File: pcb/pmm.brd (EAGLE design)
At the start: 12.6 x 18 mm, 20 parts, among them IC3 STM32F042F4, SW3 324_SW, SW4 324_SW, U2 USBC_16P, U4 XC6206_DEV

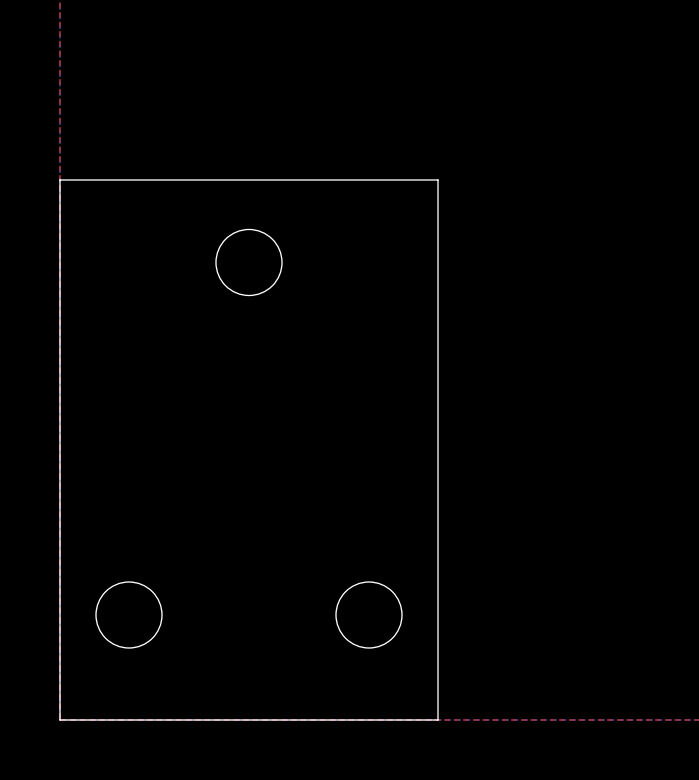
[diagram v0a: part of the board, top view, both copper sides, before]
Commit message: hotshoe done
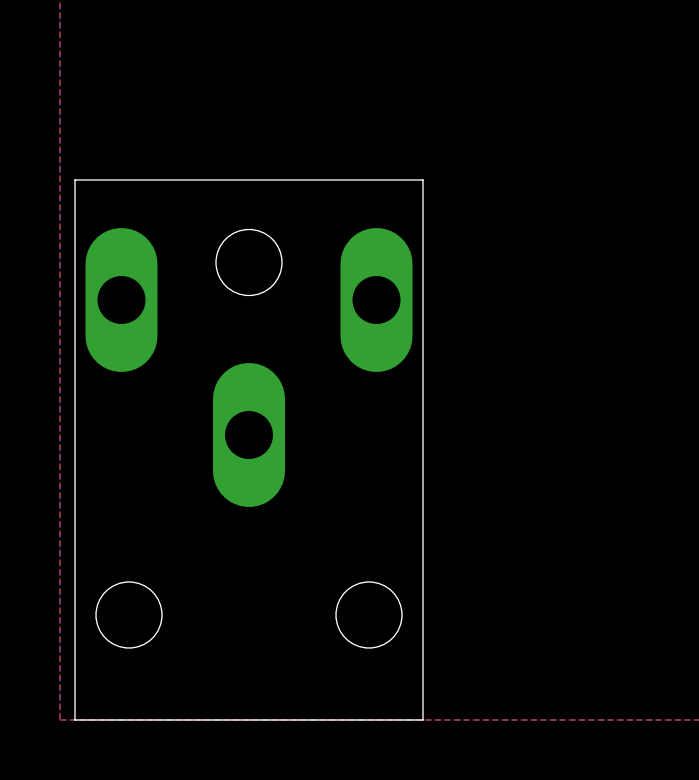
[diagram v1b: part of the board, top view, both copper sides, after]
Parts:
- added U$3, U$4, U$5: POGO_1.5MM_HOLE, apricot:POGO_1.5
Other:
- board size 12.6 x 18 mm -> 11.6 x 18 mm
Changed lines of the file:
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@@
 <setting verticaltext="up"/>
 </settings>
-<grid distance="1" unitdist="mm" unit="mm" style="lines" multiple="1" display="no" altdistance="1" altunitdist="mil" altunit="mil"/>
+<grid distance="0.5" unitdist="mm" unit="mm" style="lines" multiple="1" display="no" altdistance="1" altunitdist="mil" altunit="mil"/>
 <layers>
 <layer number="1" name="Top" color="4" fill="1" visible="no" active="yes"/>
@@
 <layer number="117" name="secv21" color="7" fill="1" visible="no" active="yes"/>
 <layer number="118" name="Rect_Pads" color="7" fill="1" visible="no" active="yes"/>
+<layer number="119" name="PF_Ref" color="7" fill="1" visible="yes" active="yes"/>
 <layer number="120" name="120" color="7" fill="1" visible="no" active="yes"/>
 <layer number="121" name="_tsilk" color="7" fill="1" visible="no" active="yes"/>
@@
 <layer number="131" name="tAdjust" color="7" fill="1" visible="no" active="yes"/>
 <layer number="132" name="bAdjust" color="7" fill="1" visible="no" active="yes"/>
+<layer number="133" name="bottom_silk" color="7" fill="1" visible="yes" active="yes"/>
+<layer number="134" name="silk_top" color="7" fill="1" visible="yes" active="yes"/>
+<layer number="135" name="silk_bottom" color="7" fill="1" visible="yes" active="yes"/>
+<layer number="136" name="silktop" color="7" fill="1" visible="yes" active="yes"/>
+<layer number="137" name="silkbottom" color="7" fill="1" visible="yes" active="yes"/>
+<layer number="138" name="EEE" color="7" fill="1" visible="yes" active="yes"/>
+<layer number="139" name="_tKeepout" color="7" fill="1" visible="yes" active="yes"/>
+<layer number="140" name="mbKeepout" color="7" fill="1" visible="yes" active="yes"/>
+<layer number="141" name="ASSEMBLY_TOP" color="7" fill="1" visible="yes" active="yes"/>
+<layer number="142" name="mbRestrict" color="7" fill="1" visible="yes" active="yes"/>
+<layer number="143" name="PLACE_BOUND_TOP" color="7" fill="1" visible="yes" active="yes"/>
 <layer number="144" name="Drill_legend" color="7" fill="1" visible="no" active="yes"/>
 <layer number="145" name="DrillLegend_01-02" color="7" fill="1" visible="no" active="yes"/>
@@
 <layer number="154" name="FabDoc2" color="7" fill="1" visible="no" active="yes"/>
 <layer number="155" name="FabDoc3" color="7" fill="1" visible="no" active="yes"/>
+<layer number="166" name="AntennaArea" color="7" fill="1" visible="yes" active="yes"/>
+<layer number="168" name="4mmHeightArea" color="7" fill="1" visible="yes" active="yes"/>
+<layer number="191" name="mNets" color="7" fill="1" visible="yes" active="yes"/>
+<layer number="192" name="mBusses" color="7" fill="1" visible="yes" active="yes"/>
+<layer number="193" name="mPins" color="7" fill="1" visible="yes" active="yes"/>
+<layer number="194" name="mSymbols" color="7" fill="1" visible="yes" active="yes"/>
+<layer number="195" name="mNames" color="7" fill="1" visible="yes" active="yes"/>
+<layer number="196" name="mValues" color="7" fill="1" visible="yes" active="yes"/>
 <layer number="199" name="Contour" color="7" fill="1" visible="no" active="yes"/>
 <layer number="200" name="200bmp" color="1" fill="10" visible="no" active="no"/>
@@
 <layer number="250" name="Descript" color="3" fill="1" visible="no" active="no"/>
 <layer number="251" name="SMDround" color="12" fill="11" visible="no" active="no"/>
+<layer number="253" name="Extra" color="7" fill="1" visible="yes" active="yes"/>
 <layer number="254" name="cooling" color="7" fill="1" visible="no" active="yes"/>
 <layer number="255" name="routoute" color="7" fill="1" visible="no" active="yes"/>
@@
 <board>
 <plain>
-<wire x1="0" y1="18" x2="0" y2="0" width="0" layer="20"/>
-<wire x1="0" y1="0" x2="12.6" y2="0" width="0" layer="20"/>
-<wire x1="12.6" y1="0" x2="12.6" y2="18" width="0" layer="20"/>
-<wire x1="12.6" y1="18" x2="0" y2="18" width="0" layer="20"/>
+<wire x1="0.5" y1="18" x2="0.5" y2="0" width="0" layer="20"/>
+<wire x1="0.5" y1="0" x2="12.1" y2="0" width="0" layer="20"/>
+<wire x1="12.1" y1="0" x2="12.1" y2="18" width="0" layer="20"/>
+<wire x1="12.1" y1="18" x2="0.5" y2="18" width="0" layer="20"/>
 <text x="60.325" y="54.61" size="0.889" layer="25">SCL</text>
 <text x="57.658" y="54.61" size="0.889" layer="25">SDA</text>
@@
 <attribute name="NAME" x="51.6852" y="49.5605" size="0.8128" layer="25"/>
 </element>
-<element name="U$12" library="3pos_slide_switch_centered" package="M2_SCREW_FOOT" value="M2_SCREW_DEV" x="6.3" y="15.25" smashed="yes"/>
-<element name="U$1" library="3pos_slide_switch_centered" package="M2_SCREW_FOOT" value="M2_SCREW_DEV" x="10.3" y="3.5" smashed="yes"/>
-<element name="U$2" library="3pos_slide_switch_centered" package="M2_SCREW_FOOT" value="M2_SCREW_DEV" x="2.3" y="3.5" smashed="yes"/>
+<element name="U$12" library="3pos_slide_switch_centered" package="M2_SCREW_FOOT" value="M2_SCREW_DEV" x="6.3" y="15.25" locked="yes" smashed="yes"/>
+<element name="U$1" library="3pos_slide_switch_centered" package="M2_SCREW_FOOT" value="M2_SCREW_DEV" x="10.3" y="3.5" locked="yes" smashed="yes"/>
+<element name="U$2" library="3pos_slide_switch_centered" package="M2_SCREW_FOOT" value="M2_SCREW_DEV" x="2.3" y="3.5" locked="yes" smashed="yes"/>
+<element name="U$3" library="apricot" package="POGO_1.5" value="POGO_1.5MM_HOLE" x="6.3" y="9.5" locked="yes" smashed="yes"/>
+<element name="U$4" library="apricot" package="POGO_1.5" value="POGO_1.5MM_HOLE" x="2.05" y="14" locked="yes" smashed="yes"/>
+<element name="U$5" library="apricot" package="POGO_1.5" value="POGO_1.5MM_HOLE" x="10.55" y="14" locked="yes" smashed="yes"/>
 </elements>
 <signals>

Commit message: working on PCB
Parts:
- added BT1: BU2032SM-G, BU2032SM-G:BAT_BU2032SM-G
- added C20, C21: 1uF, clock:0805
- added C22, C23: 2.2uF, clock:0805
- added J1: AUDIO_JACK_3.5MM_PTH, SparkFun-Connectors:AUDIO-JACK
- added J2: FFC3B07-05-T, FFC3B07-05-T:GCT_FFC3B07-05-T
- added R7: 390K, SparkFun-Passives:0805
- added R8: 5.1K, joyAnalog:0805
- added SW1: (no value), tx:SWITCH-SPST-SMD-A
- added U1: (no value), lul:LUL_UG-2864HSWEG01_1.3_WRAPAROUND
- C1, C2, C4: device clock:0805@1 -> clock:0805
- moved U2 73.6 mm to (52.7, -7.11), turned to 90 degrees
- moved LED2 2.92 mm to (48.2, 68.3)
- moved C2 2.92 mm to (63.4, 50.1)
- moved C4 2.92 mm to (66.5, 64.6)
- moved R6 2.92 mm to (48.1, 66.2)
- moved C1 2.92 mm to (66.5, 70.6)
- moved IC3 2.92 mm to (58.2, 48.3)
- moved LED1 2.92 mm to (48.2, 61.3)
- moved LED3 2.92 mm to (48.2, 54.3)
- moved R1 2.92 mm to (54.3, 62.5)
- moved R2 2.92 mm to (62.5, 62.5)
- moved R3 2.92 mm to (48.2, 52.3)
- moved R4 2.92 mm to (48.2, 59.3)
- moved R5 2.92 mm to (52.7, 47.3)
- moved SW3 2.92 mm to (68.2, 47.3)
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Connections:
- new net N$12: U1.12
- new net N$14: U1.11
- new net N$16: U1.10
- new net N$35: C20.2, U1.1
- new net N$36: C20.1, U1.2
- new net N$37: C21.2, U1.3
- new net N$38: C21.1, U1.4
- new net N$39: R7.2, U1.13
- new net N$40: C22.2, U1.14
- new net N$41: C23.2, U1.15
- new net N$43: R8.1, U1.9
- net +3V3: now also U1.5, U1.7
- net GND: now also C22.1, C23.1, R7.1, R8.2, U1.16, U1.17, U1.6
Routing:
- net N$6: track 35.6 -> 0.00 mm
- net +3V3: track 22.3 -> 0.00 mm, vias 5 -> 0
- net USB_DP: track 21.9 -> 0.00 mm
- net BUTTON1: track 19.9 -> 0.00 mm
- net USB_DN: track 19.9 -> 0.00 mm
- net +5V: track 19.0 -> 0.00 mm
- net N$4: track 15.9 -> 0.00 mm, vias 1 -> 0
- net BUTTON2: track 11.6 -> 0.00 mm
- net N$3: track 10.9 -> 0.00 mm, vias 1 -> 0
- net GND: track 5.07 -> 0.00 mm
- net N$33: track 3.52 -> 0.00 mm
- net N$31: track 2.87 -> 0.00 mm
- net N$29: track 2.14 -> 0.00 mm
- net N$5: track 2.06 -> 0.00 mm
- net N$1: track 2.06 -> 0.00 mm
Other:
- board size 11.6 x 18 mm -> 95.5 x 43 mm

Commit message: working on PCB
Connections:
- net N$16 renamed OLED_DC
- net N$3 renamed SWCLK
- net N$4 renamed SWDIO
- net N$43 renamed OLED_RESET
- net N$6 renamed UART2_TX
- removed net N$12: U1.12
- removed net N$14: U1.11
- new net OLED_CS: U1.8
- new net OLED_MOSI: IC3.13, U1.12
- new net OLED_SCK: IC3.11, U1.11
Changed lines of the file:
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@@
 <wire x1="49.058" y1="52.305" x2="49.208" y2="54.305" width="0" layer="19" extent="1-1"/>
 </signal>
-<signal name="N$3">
+<signal name="SWCLK">
 <contactref element="IC3" pad="20"/>
 </signal>
-<signal name="N$4">
+<signal name="SWDIO">
 <contactref element="IC3" pad="19"/>
-</signal>
-<signal name="N$6">
-<contactref element="IC3" pad="8"/>
 </signal>
 <signal name="N$35">
@@
 <wire x1="35.6" y1="-6.1" x2="107.4" y2="16" width="0" layer="19" extent="1-1"/>
 </signal>
-<signal name="N$43">
+<signal name="OLED_RESET">
 <contactref element="U1" pad="9"/>
 <contactref element="R8" pad="1"/>
 <wire x1="35.6" y1="-9.1" x2="83.6" y2="31.5" width="0" layer="19" extent="1-1"/>
 </signal>
-<signal name="N$12">
+<signal name="UART2_TX">
+<contactref element="IC3" pad="8"/>
+</signal>
+<signal name="OLED_MOSI">
 <contactref element="U1" pad="12"/>
+<contactref element="IC3" pad="13"/>
+<wire x1="35.6" y1="-7.6" x2="61.0758" y2="46.68" width="0" layer="19" extent="1-1"/>
 </signal>
-<signal name="N$14">
+<signal name="OLED_SCK">
 <contactref element="U1" pad="11"/>
+<contactref element="IC3" pad="11"/>
+<wire x1="35.6" y1="-8.1" x2="61.0758" y2="45.38" width="0" layer="19" extent="1-1"/>
 </signal>
-<signal name="N$16">
+<signal name="OLED_DC">
 <contactref element="U1" pad="10"/>
 </signal>
+<signal name="OLED_CS">
+<contactref element="U1" pad="8"/>
+</signal>
 </signals>

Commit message: working on PCB
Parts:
- added U$6: PINHD5, adafruit_changed:1X05
- moved C23 137.5 mm to (-27.6, -14.5)
- moved C22 133.2 mm to (-27.6, -12.7)
- moved C21 127.5 mm to (-26.9, -6.73), turned to 90 degrees
- moved R8 123.3 mm to (-31.9, -9.14), turned to 90 degrees
- moved C4 120.1 mm to (-29.0, -8.26), turned to 270 degrees
- moved C20 119.7 mm to (-25.8, -4.06)
- moved R7 116.3 mm to (-27.6, -11.0)
- moved R5 92.7 mm to (-11.1, -20.0), turned to 270 degrees
- moved C1 87.2 mm to (35.8, -11.0), turned to 0 degrees
- moved SW4 86.3 mm to (-5.80, -20.0), turned to 180 degrees
- moved SW3 83.7 mm to (18.4, -20.0)
- moved U4 80.6 mm to (35.2, -6.73), turned to 180 degrees
- moved R2 76.7 mm to (35.8, -9.40), turned to 180 degrees
- moved R1 68.6 mm to (35.8, -3.56)
- moved IC3 68.0 mm to (28.6, -13.0), turned to 0 degrees
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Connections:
- net GND: now also U$4.P$1, U$5.P$1, U$6.5
- net SWCLK: now also U$6.2
- net SWDIO: now also U$6.3
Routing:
- net OLED_MOSI: track 0.00 -> 62.5 mm
- net OLED_SCK: track 0.00 -> 57.6 mm
- net BUTTON2: track 0.00 -> 41.7 mm
- net USB_DP: track 0.00 -> 35.7 mm
- net +3V3: track 0.00 -> 29.9 mm, vias 0 -> 5
- net USB_DN: track 0.00 -> 18.0 mm
- net +5V: track 0.00 -> 16.0 mm
- net BUTTON1: track 0.00 -> 15.6 mm
- net GND: track 0.00 -> 12.7 mm
- net OLED_RESET: track 0.00 -> 7.50 mm
- net SWCLK: track 0.00 -> 7.01 mm
- net SWDIO: track 0.00 -> 6.23 mm
- net N$36: track 0.00 -> 3.98 mm
- net N$31: track 0.00 -> 3.56 mm
- net N$33: track 0.00 -> 3.19 mm
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- added copper zone on layer 16, net GND
- removed copper zone on layer 16, net +3V3
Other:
- board size 95.5 x 43 mm -> 81.6 x 43 mm
- board text removed: "GND"
- board text removed: "RX"
- board text removed: "SCL"
- board text removed: "SDA"
- board text removed: "VCC"

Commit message: working on PCB
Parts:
- removed LED2, LED3: (no value), adafruit:CHIP-LED0805
- removed R3, R6: 1K, SparkFun-Passives:0805
- removed SW1: (no value), tx:SWITCH-SPST-SMD-A
- added JP1: (no value), adafruit_changed:1X03-CLEANBIG
- added U$7: PINHD1X4, adafruit_changed:1X04-CLEANBIG
- moved LED1 83.4 mm to (31.3, -20.4)
- moved R4 83.4 mm to (31.3, -22.4)
- moved BT1 1.10 mm to (-17.6, -13.5), turned to 0 degrees
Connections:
- removed net N$1: LED3.C, R3.2
- removed net N$29: LED2.C, R6.2
- new net LIGHT_SENSE: J2.3
- new net N$2: IC3.14, U$3.P$1, U$7.2, U$7.3
- new net N$3: BT1.+, JP1.2
- net +3V3: now also J2.2, J2.4, JP1.3; no longer LED2.A, LED3.A
- net GND: now also BT1.-, J2.1, J2.5, J2.S1, J2.S2, U$7.1, U$7.4; no longer R6.1
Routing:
- net +3V3: track 29.9 -> 111.6 mm, vias 5 -> 7
- net N$2: track 0.00 -> 44.4 mm
- net N$3: track 0.00 -> 13.3 mm
- net OLED_SCK: track 57.6 -> 58.3 mm
- net OLED_MOSI: track 62.5 -> 63.2 mm
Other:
- board text added: "GND"
- board text added: "TRIG"

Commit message: working on PCB
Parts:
- added JP2, JP3: (no value), pinhead:1X02
- moved R4 2.32 mm to (29.0, -22.7)
- moved LED1 1.85 mm to (29.5, -20.9)
- moved J1 0.20 mm to (43.7, -18.7)
- moved JP1 0.13 mm to (6.30, -20.4)
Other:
- board text added: "middle pin on 3v3, left pin coin battery, right pin regulator output move regulator down twoards the edge"
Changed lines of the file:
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@@
 <text x="2.3944" y="-0.6862" size="1.27" layer="25" rot="R270" align="center">GND</text>
 <rectangle x1="3.231" y1="-22.468" x2="6.731" y2="-18.968" layer="51"/>
+<text x="-30.48" y="-29.083" size="1.778" layer="21">middle pin on 3v3, left pin coin battery, right pin regulator output
+move regulator down twoards the edge</text>
 </plain>
 <attributes>
@@
 <element name="SW3" library="3pos_slide_switch_centered" package="342_SWICH_FOOT" value="324_SW" x="18.4" y="-20" smashed="yes" rot="R180"/>
 <element name="SW4" library="3pos_slide_switch_centered" package="342_SWICH_FOOT" value="324_SW" x="-5.8" y="-20" smashed="yes" rot="R180"/>
-<element name="LED1" library="adafruit" package="CHIP-LED0805" value="" x="31.267" y="-20.356" smashed="yes" rot="R270">
-<attribute name="VALUE" x="29.997" y="-22.896" size="1.27" layer="27"/>
-</element>
-<element name="R4" library="SparkFun-Passives" package="0805" value="1K" x="31.267" y="-22.356" smashed="yes">
-<attribute name="NAME" x="32.8164" y="-23.2069" size="0.8128" layer="25"/>
+<element name="LED1" library="adafruit" package="CHIP-LED0805" value="" x="29.489" y="-20.864" smashed="yes" rot="R270">
+<attribute name="VALUE" x="28.219" y="-23.404" size="1.27" layer="27"/>
+</element>
+<element name="R4" library="SparkFun-Passives" package="0805" value="1K" x="28.981" y="-22.737" smashed="yes">
+<attribute name="NAME" x="30.5304" y="-23.5879" size="0.8128" layer="25"/>
 </element>
 <element name="R5" library="joyAnalog" package="0805" value="5.1K" x="-11.1286" y="-20" smashed="yes" rot="R270">
@@
 <attribute name="SNAPEDA_LINK" value="https://www.snapeda.com/parts/BU2032SM-G/Memory+Protection+Devices/view-part/?ref=snap" x="-17.6" y="-13.5" size="1.778" layer="28" rot="MR0" display="off"/>
 </element>
-<element name="J1" library="SparkFun-Connectors" package="AUDIO-JACK" value="AUDIO_JACK_3.5MM_PTH" x="43.873" y="-18.735" smashed="yes" rot="R180">
-<attribute name="PROD_ID" value="CONN-08774" x="43.873" y="-18.735" size="1.778" layer="27" rot="R180" display="off"/>
-<attribute name="SF_ID" value="PRT-08032" x="43.873" y="-18.735" size="1.778" layer="27" rot="R180" display="off"/>
+<element name="J1" library="SparkFun-Connectors" package="AUDIO-JACK" value="AUDIO_JACK_3.5MM_PTH" x="43.688" y="-18.669" smashed="yes" rot="R180">
+<attribute name="PROD_ID" value="CONN-08774" x="43.688" y="-18.669" size="1.778" layer="27" rot="R180" display="off"/>
+<attribute name="SF_ID" value="PRT-08032" x="43.688" y="-18.669" size="1.778" layer="27" rot="R180" display="off"/>
 </element>
 <element name="J2" library="FFC3B07-05-T" package="GCT_FFC3B07-05-T" value="FFC3B07-05-T" x="-27.813" y="-20.701" smashed="yes">
@@
 <element name="U$6" library="adafruit_changed" package="1X05" value="PINHD5" x="27.559" y="-3.81" smashed="yes"/>
 <element name="U$7" library="adafruit_changed" package="1X04-CLEANBIG" value="PINHD1X4" x="6.223" y="-3.683" smashed="yes"/>
-<element name="JP1" library="adafruit_changed" package="1X03-CLEANBIG" value="" x="6.3" y="-20.5" smashed="yes">
-<attribute name="VALUE" x="2.49" y="-23.675" size="1.27" layer="27"/>
+<element name="JP1" library="adafruit_changed" package="1X03-CLEANBIG" value="" x="6.3" y="-20.373" smashed="yes">
+<attribute name="VALUE" x="2.49" y="-23.548" size="1.27" layer="27"/>
+</element>
+<element name="JP2" library="pinhead" library_urn="urn:adsk.eagle:library:325" package="1X02" package3d_urn="urn:adsk.eagle:package:22435/2" value="" x="-17.653" y="-23.241" smashed="yes" rot="R180">
+<attribute name="POPULARITY" value="98" x="-17.653" y="-23.241" size="1.778" layer="27" rot="R180" display="off"/>
+<attribute name="VALUE" x="-15.113" y="-20.066" size="1.27" layer="27" rot="R180"/>
+</element>
+<element name="JP3" library="pinhead" library_urn="urn:adsk.eagle:library:325" package="1X02" package3d_urn="urn:adsk.eagle:package:22435/2" value="" x="34.036" y="-21.717" smashed="yes" rot="R90">
+<attribute name="POPULARITY" value="98" x="34.036" y="-21.717" size="1.778" layer="27" rot="R90" display="off"/>
+<attribute name="VALUE" x="37.211" y="-24.257" size="1.27" layer="27" rot="R90"/>
 </element>
 </elements>
@@
 <wire x1="-26.813" y1="-20.05" x2="-26.797" y2="-20.066" width="0.508" layer="1"/>
 <contactref element="JP1" pad="3"/>
-<wire x1="28.321" y1="-14.478" x2="14.862" y2="-14.478" width="0.508" layer="16"/>
-<wire x1="14.862" y1="-14.478" x2="8.84" y2="-20.5" width="0.508" layer="16"/>
-<wire x1="8.84" y1="-20.5" x2="7.3436" y2="-21.9964" width="0.508" layer="16"/>
+<wire x1="28.321" y1="-14.478" x2="14.735" y2="-14.478" width="0.508" layer="16"/>
+<wire x1="14.735" y1="-14.478" x2="8.84" y2="-20.373" width="0.508" layer="16"/>
+<wire x1="8.84" y1="-20.373" x2="7.3436" y2="-21.8694" width="0.508" layer="16"/>
 <wire x1="-2.794" y1="-18.923" x2="-5.842" y2="-18.923" width="0.508" layer="16"/>
-<wire x1="7.3436" y1="-21.9964" x2="0.2794" y2="-21.9964" width="0.508" layer="16"/>
-<wire x1="0.2794" y1="-21.9964" x2="-2.794" y2="-18.923" width="0.508" layer="16"/>
+<wire x1="7.3436" y1="-21.8694" x2="0.1524" y2="-21.8694" width="0.508" layer="16"/>
+<wire x1="0.1524" y1="-21.8694" x2="-2.794" y2="-18.923" width="0.508" layer="16"/>
 <wire x1="-8" y1="-18.875" x2="-5.89" y2="-18.875" width="0.508" layer="1"/>
 <wire x1="-5.89" y1="-18.875" x2="-5.842" y2="-18.923" width="0.508" layer="1"/>
@@
 <wire x1="-28.829" y1="-20.066" x2="-28.829" y2="-10.795" width="0.508" layer="16"/>
 <wire x1="-28.829" y1="-10.795" x2="-30.48" y2="-9.144" width="0.508" layer="16"/>
-<wire x1="28.25" y1="-15.8718" x2="30.217" y2="-20.356" width="0" layer="19" extent="1-1"/>
+<wire x1="28.25" y1="-15.8718" x2="28.439" y2="-20.864" width="0" layer="19" extent="1-1"/>
 </signal>
 <signal name="USB_DP">
@@
 <contactref element="LED1" pad="C"/>
 <contactref element="R4" pad="2"/>
-<wire x1="32.167" y1="-22.356" x2="32.317" y2="-20.356" width="0" layer="19" extent="1-1"/>
+<wire x1="29.881" y1="-22.737" x2="30.539" y2="-20.864" width="0" layer="19" extent="1-1"/>
 </signal>
 <signal name="SWCLK">
@@
 <contactref element="JP1" pad="2"/>
 <wire x1="-3.1" y1="-13.5" x2="1.054" y2="-13.5" width="0.508" layer="16"/>
-<wire x1="6.3" y1="-18.746" x2="6.3" y2="-20.5" width="0.508" layer="16"/>
+<wire x1="6.3" y1="-18.746" x2="6.3" y2="-20.373" width="0.508" layer="16"/>
 <wire x1="1.054" y1="-13.5" x2="6.3" y2="-18.746" width="0.508" layer="16"/>
 </signal>
@@
 </board>
 </drawing>
+<compatibility>
+<note version="6.3" minversion="6.2.2" severity="warning">
+Since Version 6.2.2 text objects can contain more than one line,
+which will not be processed correctly with this version.
+</note>
+<note version="8.2" severity="warning">
+Since Version 8.2, EAGLE supports online libraries. The ids
+of those online libraries will not be understood (or retained)
+with this version.
+</note>
+<note version="8.3" severity="warning">
+Since Version 8.3, EAGLE supports URNs for individual library
+assets (packages, symbols, and devices). The URNs of those assets
+will not be understood (or retained) with this version.
+</note>
+<note version="8.3" severity="warning">
+Since Version 8.3, EAGLE supports the association of 3D packages
+with devices in libraries, schematics, and board files. Those 3D
+packages will not be understood (or retained) with this version.
+</note>
+</compatibility>
 </eagle>
